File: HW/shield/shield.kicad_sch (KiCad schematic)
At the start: 70 parts

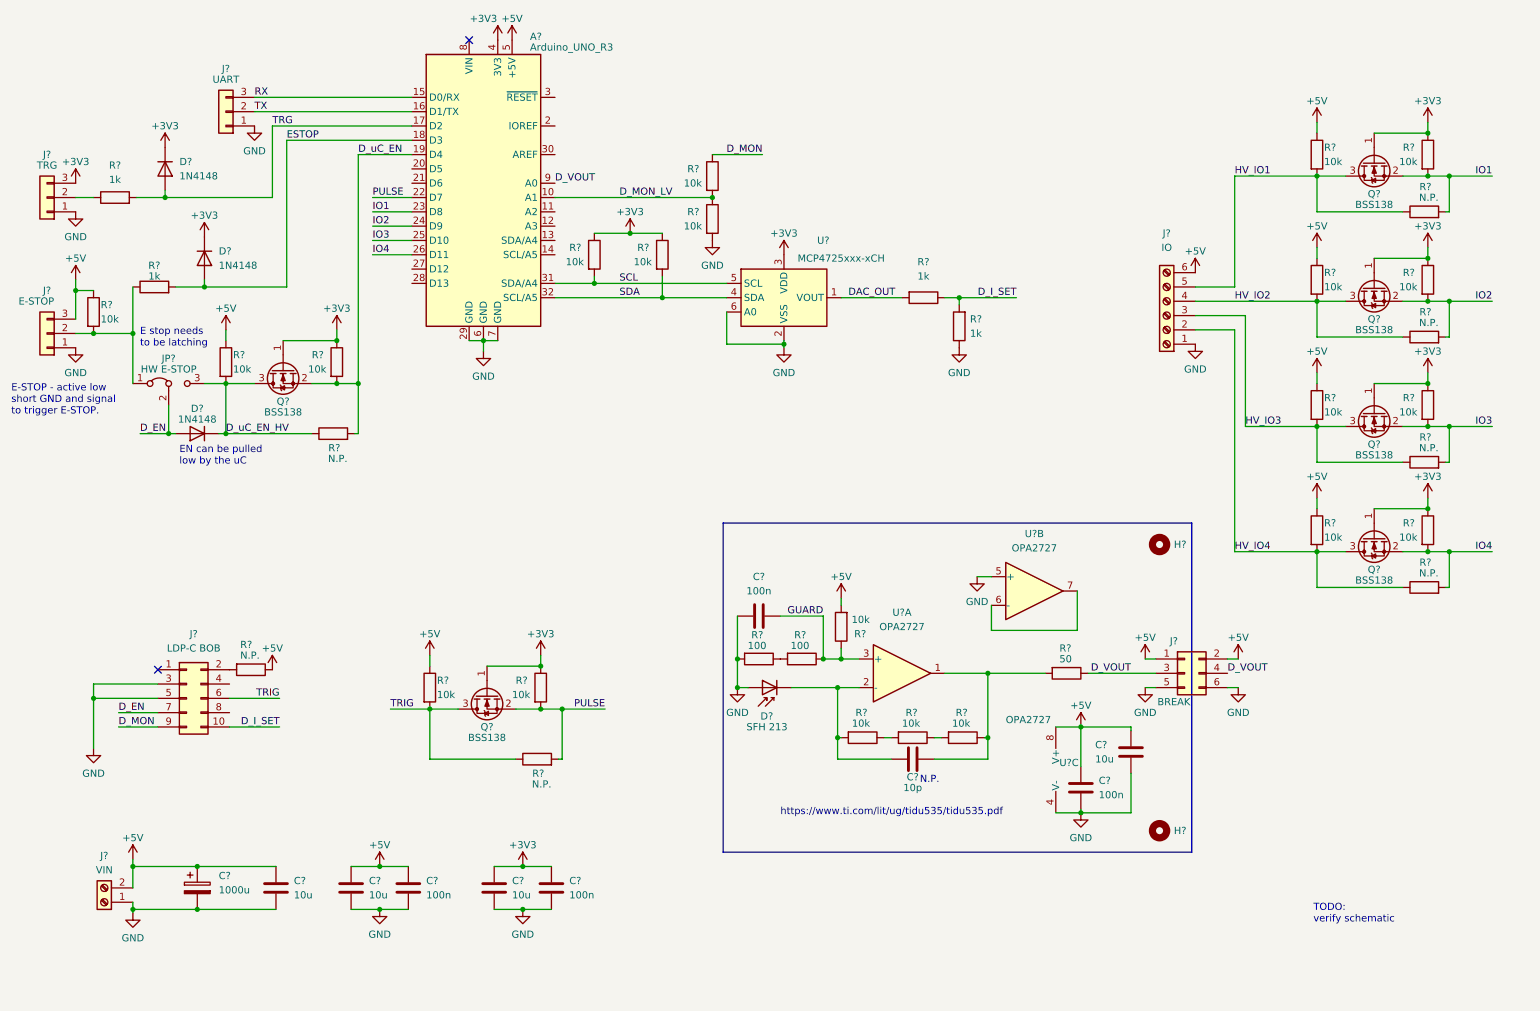
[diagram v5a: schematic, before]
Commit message: added rudamentary pulse generation
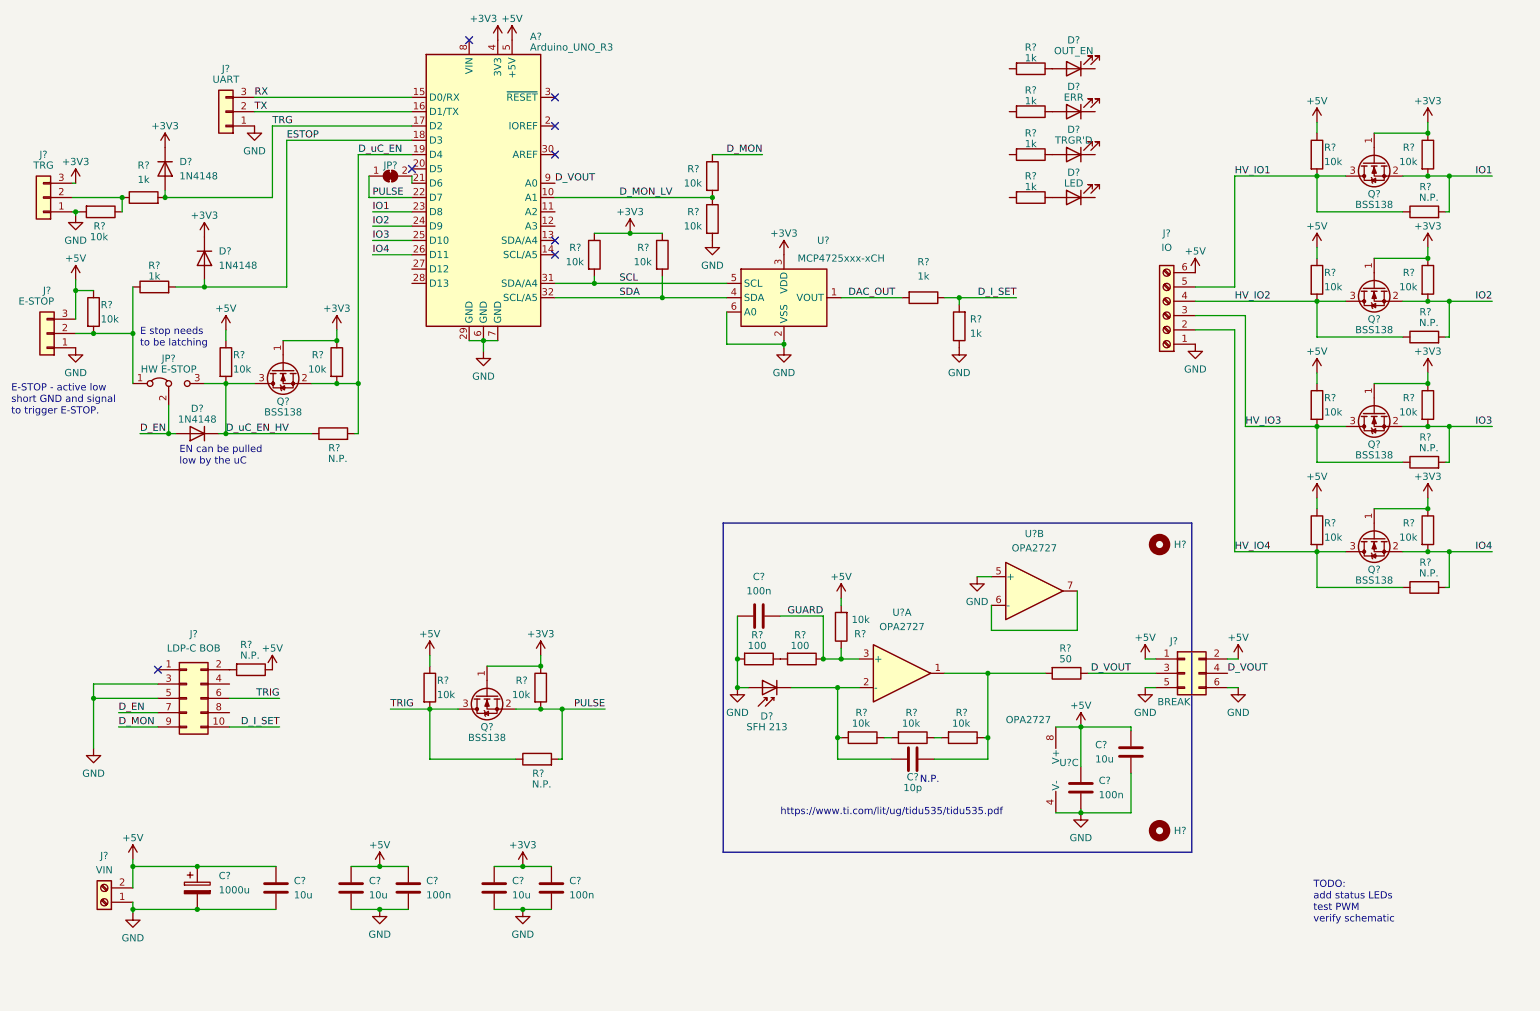
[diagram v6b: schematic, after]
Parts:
- added D?: ERR, symbol Device:LED
- added D?: TRGR'D, symbol Device:LED
- added D?: LED, symbol Device:LED
- added D?: OUT_EN, symbol Device:LED
- added JP?: INTR, symbol Jumper:SolderJumper_2_Bridged
- added R?: 10k, symbol Device:R
- added R? (x4): 1k, symbol Device:R
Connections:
- net GND: now also R?.2
- net PULSE: now also JP?.1 (A)
- net at J?.2 (Pin_2), R?.1: now also R?.1
- net at A?.21 (D6): now also JP?.2 (B)
- new net: D?.2 (A), R?.1 (x4)
- no-connect marks 2 -> 8
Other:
- note added: "TODO: add status LEDs test PWM verify schematic"
- note removed: "TODO: verify schematic"
- moved on the sheet: J?, R?

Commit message: started PCB
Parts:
- removed J?: TRG, symbol Connector_Generic:Conn_01x03
- added J1: TRG, Connector_Coaxial:SMA_Amphenol_901-144_Vertical, symbol Connector:Conn_Coaxial
- C1: renamed from C?; footprint (none) -> Capacitor_SMD:CP_Elec_10x10
- C10, C2, C3, C4, C5, C6, C7, C8, C9: renamed from C?; footprint (none) -> Capacitor_SMD:C_0805_2012Metric_Pad1.18x1.45mm_HandSolder
- D1, D2, D3: renamed from D?; footprint (none) -> Diode_SMD:D_SOD-123
- D4, D5, D6, D7: renamed from D?; footprint (none) -> LED_SMD:LED_0805_2012Metric_Pad1.15x1.40mm_HandSolder
- D8: renamed from D?; footprint (none) -> LED_THT:LED_D5.0mm_IRGrey
- H1, H2: renamed from H?; footprint (none) -> MountingHole:MountingHole_3.2mm_M3
- J2: renamed from J?; footprint (none) -> TerminalBlock:TerminalBlock_Altech_AK300-3_P5.00mm
- J3: renamed from J?; footprint (none) -> Connector_PinSocket_2.54mm:PinSocket_1x03_P2.54mm_Vertical
- J4: renamed from J?; footprint (none) -> TerminalBlock_Altech:Altech_AK300_1x06_P5.00mm_45-Degree
- J5: renamed from J?; footprint (none) -> Connector_PinHeader_2.54mm:PinHeader_2x05_P2.54mm_Vertical
- J6: renamed from J?; footprint (none) -> TerminalBlock:TerminalBlock_Altech_AK300-2_P5.00mm
- J7: renamed from J?; footprint (none) -> Connector_PinSocket_2.54mm:PinSocket_2x03_P2.54mm_Vertical
- JP1: renamed from JP?; footprint (none) -> Jumper:SolderJumper-3_P1.3mm_Bridged12_RoundedPad1.0x1.5mm_NumberLabels
- JP2: renamed from JP?; footprint (none) -> Jumper:SolderJumper-2_P1.3mm_Open_RoundedPad1.0x1.5mm
- R1, R10, R11, R12, R13, R14, R15, R16, R17, R18, R19, R20, R21, R22, R23, R24, R25, R26, R27, R28, R29, R3, R30, R31, R32, R33, R34, R35, R36, R37, R38, R39, R4, R40, R5, R6, R7, R8, R9: renamed from R?; footprint (none) -> Resistor_SMD:R_0805_2012Metric_Pad1.20x1.40mm_HandSolder
- R2: renamed from R?; value 10k -> 50; footprint (none) -> Resistor_SMD:R_0805_2012Metric_Pad1.20x1.40mm_HandSolder
- U2: renamed from U?; footprint Package_SO:MSOP-8_3x3mm_P0.65mm -> Package_SO:SO-8_3.9x4.9mm_P1.27mm
- gave numbers to parts that had none: 8
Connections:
- net GND: now also D4.1 (K), D5.1 (K), D6.1 (K), D7.1 (K), J1.2 (Ext)
- net GUARDED: now reaches C9.1, D8.1 (K), R38.2, U2.2 (-)
- net at R2.1, R3.1: now also J1.1 (In)
- net LED4: now reaches R17.2
- net LED4: now also A1.28 (D13)
- net LED3: now reaches R16.2
- net LED3: now also A1.27 (D12)
- net LED1: now reaches R14.2
- net LED1: now also A1.12 (A3)
- net LED2: now reaches R15.2
- net LED2: now also A1.11 (A2)
- net GUARD: no longer names the net of C7.2, R34.1, R36.1, U2.3 (+)
- no-connect marks 8 -> 10
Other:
- note added: "TODO:"
- note removed: "TODO: add status LEDs test PWM verify schematic"
- moved on the sheet: R2

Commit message: improved guard
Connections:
- net GND: no longer U2.5 (+)
- net GUARDED: now also U2.5 (+)
- net GUARD: now reaches U2.6 (-), U2.7
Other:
- moved on the sheet: R37
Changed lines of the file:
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@@
     (stroke (width 0) (type default) (color 0 0 0 0))
   )
-  (wire (pts (xy 209.55 132.715) (xy 221.615 132.715))
+  (wire (pts (xy 215.265 132.715) (xy 221.615 132.715))
     (stroke (width 0) (type default) (color 0 0 0 0))
   )
@@
     (stroke (width 0) (type default) (color 0 0 0 0))
   )
+  (wire (pts (xy 183.515 115.57) (xy 192.405 115.57))
+    (stroke (width 0) (type default) (color 0 0 0 0))
+  )
   (wire (pts (xy 265.43 44.45) (xy 269.875 44.45))
     (stroke (width 0) (type default) (color 0 0 0 0))
@@
     (stroke (width 0) (type default) (color 0 0 0 0))
   )
-  (wire (pts (xy 189.865 115.57) (xy 192.405 115.57))
-    (stroke (width 0) (type default) (color 0 0 0 0))
-  )
   (wire (pts (xy 121.92 54.61) (xy 128.27 54.61))
     (stroke (width 0) (type default) (color 0 0 0 0))
   )
-  (wire (pts (xy 191.77 132.715) (xy 201.93 132.715))
+  (wire (pts (xy 191.77 132.715) (xy 207.645 132.715))
     (stroke (width 0) (type default) (color 0 0 0 0))
   )
@@
     (effects (font (size 1.27 1.27)) (justify right bottom))
   )
-  (label "D_VOUT" (at 217.17 132.715 180)
+  (label "D_VOUT" (at 221.615 132.715 180)
     (effects (font (size 1.27 1.27)) (justify right bottom))
   )
@@
     (effects (font (size 1.27 1.27)) (justify right bottom))
   )
+  (label "GUARDED" (at 183.515 115.57 0)
+    (effects (font (size 1.27 1.27)) (justify left bottom))
+  )
   (label "LED1" (at 114.935 53.34 0)
     (effects (font (size 1.27 1.27)) (justify left bottom))
@@
   (label "TRIG" (at 66.04 137.16 180)
     (effects (font (size 1.27 1.27)) (justify right bottom))
+  )
+  (label "GUARD" (at 207.645 118.11 0)
+    (effects (font (size 1.27 1.27)) (justify left bottom))
   )
   (label "D_EN" (at 37.465 139.7 0)
@@
     (pin "1")
   )
-  (symbol (lib_id "power:GND") (at 189.865 115.57 0) (unit 1)
-    (in_bom yes) (on_board yes) (fields_autoplaced)
-    (property "Reference" "#PWR039" (id 0) (at 189.865 121.92 0)
-      (effects (font (size 1.27 1.27)) hide)
-    )
-    (property "Value" "GND" (id 1) (at 189.865 120.015 0))
-    (property "Footprint" "" (id 2) (at 189.865 115.57 0)
-      (effects (font (size 1.27 1.27)) hide)
-    )
-    (property "Datasheet" "" (id 3) (at 189.865 115.57 0)
-      (effects (font (size 1.27 1.27)) hide)
-    )
-    (pin "1")
-  )
   (symbol (lib_id "Device:R") (at 151.13 130.175 270) (unit 1)
     (in_bom yes) (on_board yes)
@@
   )
   (symbol (lib_id "Amplifier_Operational:MCP6L02x-xMS") (at 176.53 132.715 0) (unit 1)
-    (in_bom yes) (on_board yes) (fields_autoplaced)
+    (in_bom yes) (on_board yes)
     (property "Reference" "U2" (id 0) (at 176.53 121.92 0))
     (property "Value" "OPA2727" (id 1) (at 176.53 124.46 0))
@@
   )
   (symbol (lib_id "Amplifier_Operational:MCP6L02x-xMS") (at 200.025 118.11 0) (unit 2)
-    (in_bom yes) (on_board yes) (fields_autoplaced)
+    (in_bom yes) (on_board yes)
     (property "Reference" "U2" (id 0) (at 200.025 107.95 0))
     (property "Value" "OPA2727" (id 1) (at 200.025 110.49 0))
@@
     (pin "1")
   )
-  (symbol (lib_id "Device:R") (at 205.74 132.715 270) (unit 1)
-    (in_bom yes) (on_board yes)
-    (property "Reference" "R37" (id 0) (at 204.47 128.27 90)
-      (effects (font (size 1.27 1.27)) (justify left))
-    )
-    (property "Value" "50" (id 1) (at 204.47 130.175 90)
-      (effects (font (size 1.27 1.27)) (justify left))
-    )
-    (property "Footprint" "Resistor_SMD:R_0805_2012Metric_Pad1.20x1.40mm_HandSolder" (id 2) (at 205.74 130.937 90)
-      (effects (font (size 1.27 1.27)) hide)
-    )
-    (property "Datasheet" "~" (id 3) (at 205.74 132.715 0)
+  (symbol (lib_id "Device:R") (at 211.455 132.715 270) (unit 1)
+    (in_bom yes) (on_board yes)
+    (property "Reference" "R37" (id 0) (at 210.185 128.27 90)
+      (effects (font (size 1.27 1.27)) (justify left))
+    )
+    (property "Value" "50" (id 1) (at 210.185 130.175 90)
+      (effects (font (size 1.27 1.27)) (justify left))
+    )
+    (property "Footprint" "Resistor_SMD:R_0805_2012Metric_Pad1.20x1.40mm_HandSolder" (id 2) (at 211.455 130.937 90)
+      (effects (font (size 1.27 1.27)) hide)
+    )
+    (property "Datasheet" "~" (id 3) (at 211.455 132.715 0)
       (effects (font (size 1.27 1.27)) hide)
     )
@@
       (reference "#PWR038") (unit 1) (value "GND") (footprint "")
     )
-    (path "/3320a38d-40de-4d87-b877-193a4b5fe238"
-      (reference "#PWR039") (unit 1) (value "GND") (footprint "")
-    )
     (path "/775023b7-60fe-4cbf-8735-4058ca512396"
